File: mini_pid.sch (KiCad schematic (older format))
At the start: 68 parts, among them P1 PD Mon/Output, P2 Ext. Mod/SetPt Mon, U1 ED2610, U2 OPA2211, U3 LM2940, U4 OPA4227, U5 8DIP, U6 8DIP, U7 OPA2227

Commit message: Layout for old version completed
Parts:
- removed P2: Ext. Mod/SetPt Mon, footprints:Dual-BNC-ARF2136, symbol Dual-BNC
- added S3: spdt, footprints:CJS-1200TB-SPDT, symbol spdt
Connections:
- net GND: now also U4.5 (+); no longer U4.3 (+)
- net at C15.1, R3.1, R6.2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: now also U4.3 (+); no longer U4.5 (+)
- net at R22.2, S1.1: now also U4.7; no longer U4.1
- net at R20.2, R22.1: now also U4.6 (-); no longer U4.2 (-)
- net ext.mod.input: now reaches R4.1
- net ext.mod.input: now also S3.3
- new net: S3.1, U4.1, U4.2 (-)
- new net: P1.1, S3.2
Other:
- moved on the sheet: P1A
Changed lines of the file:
@@
 $Comp
 L OPA4227 U4
-U 2 1 58B790A6
+U 1 1 58B790A6
 P 4650 2800
 F 0 "U4" H 4700 3000 50  0000 C CNN
@@
 F 2 "Housings_SOIC:SOIC-14_3.9x8.7mm_Pitch1.27mm" H 4600 2900 50  0001 C CNN
 F 3 "" H 4700 3000 50  0000 C CNN
-	2    4650 2800
+	1    4650 2800
 	1    0    0    -1
 $EndComp
 $Comp
 L OPA4227 U4
-U 1 1 58B7910B
+U 2 1 58B7910B
 P 8350 2950
 F 0 "U4" H 8400 3150 50  0000 C CNN
@@
 F 2 "Housings_SOIC:SOIC-14_3.9x8.7mm_Pitch1.27mm" H 8300 3050 50  0001 C CNN
 F 3 "" H 8400 3150 50  0000 C CNN
-	1    8350 2950
+	2    8350 2950
 	1    0    0    -1
 $EndComp
@@
 $EndComp
 $Comp
-L Dual-BNC P2
-U 1 1 58B9ABD7
-P 3100 6050
-F 0 "P2" H 3100 6200 60  0000 C CNN
-F 1 "Ext. Mod/SetPt Mon" V 3300 5950 60  0000 C CNN
-F 2 "footprints:Dual-BNC-ARF2136" H 3100 6050 60  0001 C CNN
-F 3 "" H 3100 6050 60  0000 C CNN
-	1    3100 6050
-	-1   0    0    -1
-$EndComp
-$Comp
-L GND #PWR021
-U 1 1 58B9B8ED
-P 3100 6350
-F 0 "#PWR021" H 3100 6100 50  0001 C CNN
-F 1 "GND" H 3100 6200 50  0000 C CNN
-F 2 "" H 3100 6350 50  0000 C CNN
-F 3 "" H 3100 6350 50  0000 C CNN
-	1    3100 6350
-	1    0    0    -1
-$EndComp
-$Comp
 L R R4
 U 1 1 58B9BB14
@@
 $EndComp
 $Comp
-L GND #PWR022
+L GND #PWR021
 U 1 1 58B9F9E2
 P 3900 4900
-F 0 "#PWR022" H 3900 4650 50  0001 C CNN
+F 0 "#PWR021" H 3900 4650 50  0001 C CNN
 F 1 "GND" H 3900 4750 50  0000 C CNN
 F 2 "" H 3900 4900 50  0000 C CNN
@@
 L Dual-BNC P1
 U 1 1 58BA3D1D
-P 5400 2800
-F 0 "P1" H 5400 2950 60  0000 C CNN
-F 1 "PD Mon/Output" V 5600 2700 60  0000 C CNN
-F 2 "footprints:Dual-BNC-ARF2136" H 5400 2800 60  0001 C CNN
-F 3 "" H 5400 2800 60  0000 C CNN
-	1    5400 2800
-	1    0    0    -1
-$EndComp
-$Comp
-L GND #PWR023
+P 6650 2800
+F 0 "P1" H 6650 2950 60  0000 C CNN
+F 1 "PD Mon/Output" V 6850 2700 60  0000 C CNN
+F 2 "footprints:Dual-BNC-ARF2136" H 6650 2800 60  0001 C CNN
+F 3 "" H 6650 2800 60  0000 C CNN
+	1    6650 2800
+	1    0    0    -1
+$EndComp
+$Comp
+L GND #PWR022
 U 1 1 58BA4480
-P 5400 3100
-F 0 "#PWR023" H 5400 2850 50  0001 C CNN
-F 1 "GND" H 5400 2950 50  0000 C CNN
-F 2 "" H 5400 3100 50  0000 C CNN
-F 3 "" H 5400 3100 50  0000 C CNN
-	1    5400 3100
+P 6650 3200
+F 0 "#PWR022" H 6650 2950 50  0001 C CNN
+F 1 "GND" H 6650 3050 50  0000 C CNN
+F 2 "" H 6650 3200 50  0000 C CNN
+F 3 "" H 6650 3200 50  0000 C CNN
+	1    6650 3200
 	1    0    0    -1
 $EndComp
@@
 PI pole (Hz)\n48k\n16k\n7k\n3k\n1.6k\n700\n340\nOff
 $Comp
-L +15V #PWR024
+L +15V #PWR023
 U 1 1 58BB15C2
 P 5250 3650
-F 0 "#PWR024" H 5250 3500 50  0001 C CNN
+F 0 "#PWR023" H 5250 3500 50  0001 C CNN
 F 1 "+15V" H 5250 3790 50  0000 C CNN
 F 2 "" H 5250 3650 50  0000 C CNN
@@
 $EndComp
 $Comp
-L GND #PWR025
+L GND #PWR024
 U 1 1 58BB23F2
 P 5900 3700
-F 0 "#PWR025" H 5900 3450 50  0001 C CNN
+F 0 "#PWR024" H 5900 3450 50  0001 C CNN
 F 1 "GND" H 5900 3550 50  0000 C CNN
 F 2 "" H 5900 3700 50  0000 C CNN
@@
 $EndComp
 $Comp
-L GND #PWR026
+L GND #PWR025
 U 1 1 58BB3AC3
 P 5850 4600
-F 0 "#PWR026" H 5850 4350 50  0001 C CNN
+F 0 "#PWR025" H 5850 4350 50  0001 C CNN
 F 1 "GND" H 5850 4450 50  0000 C CNN
 F 2 "" H 5850 4600 50  0000 C CNN
@@
 $EndComp
 $Comp
-L -15V #PWR19
+L -15V #PWR18
 U 1 1 58BB5199
 P 4400 3350
-F 0 "#PWR19" H 4400 3450 50  0001 C CNN
+F 0 "#PWR18" H 4400 3450 50  0001 C CNN
 F 1 "-15V" H 4400 3500 50  0000 C CNN
 F 2 "" H 4400 3350 50  0000 C CNN
@@
 $EndComp
 $Comp
-L -15V #PWR32
+L -15V #PWR24
 U 1 1 58BB5F58
 P 5150 4600
-F 0 "#PWR32" H 5150 4700 50  0001 C CNN
+F 0 "#PWR24" H 5150 4700 50  0001 C CNN
 F 1 "-15V" H 5150 4750 50  0000 C CNN
 F 2 "" H 5150 4600 50  0000 C CNN
@@
 $EndComp
 $Comp
-L GND #PWR027
+L GND #PWR026
 U 1 1 58BB876C
 P 7650 2850
-F 0 "#PWR027" H 7650 2600 50  0001 C CNN
+F 0 "#PWR026" H 7650 2600 50  0001 C CNN
 F 1 "GND" H 7650 2700 50  0000 C CNN
 F 2 "" H 7650 2850 50  0000 C CNN
@@
 $EndComp
 $Comp
-L GND #PWR028
+L GND #PWR027
 U 1 1 58BBECAC
 P 7200 1550
-F 0 "#PWR028" H 7200 1300 50  0001 C CNN
+F 0 "#PWR027" H 7200 1300 50  0001 C CNN
 F 1 "GND" H 7200 1400 50  0000 C CNN
 F 2 "" H 7200 1550 50  0000 C CNN
@@
 $EndComp
 $Comp
-L GND #PWR029
-U 1 1 58BCC220
-P 5050 7000
-F 0 "#PWR029" H 5050 6750 50  0001 C CNN
-F 1 "GND" H 5050 6850 50  0000 C CNN
-F 2 "" H 5050 7000 50  0000 C CNN
-F 3 "" H 5050 7000 50  0000 C CNN
-	1    5050 7000
-	1    0    0    -1
-$EndComp
-$Comp
-L +15V #PWR030
+L +15V #PWR028
 U 1 1 58BCFB3C
 P 5950 750
-F 0 "#PWR030" H 5950 600 50  0001 C CNN
+F 0 "#PWR028" H 5950 600 50  0001 C CNN
 F 1 "+15V" H 5950 890 50  0000 C CNN
 F 2 "" H 5950 750 50  0000 C CNN
@@
 $EndComp
 $Comp
-L GND #PWR031
+L GND #PWR029
 U 1 1 58BD050F
 P 5950 1650
-F 0 "#PWR031" H 5950 1400 50  0001 C CNN
+F 0 "#PWR029" H 5950 1400 50  0001 C CNN
 F 1 "GND" H 5950 1500 50  0000 C CNN
 F 2 "" H 5950 1650 50  0000 C CNN
@@
 $EndComp
 $Comp
-L GND #PWR032
+L GND #PWR030
 U 1 1 58BDFB40
 P 10850 4600
-F 0 "#PWR032" H 10850 4350 50  0001 C CNN
+F 0 "#PWR030" H 10850 4350 50  0001 C CNN
 F 1 "GND" H 10850 4450 50  0000 C CNN
 F 2 "" H 10850 4600 50  0000 C CNN
@@
 $EndComp
 $Comp
-L PWR_FLAG #FLG033
+L PWR_FLAG #FLG031
 U 1 1 58BE3FE5
 P 1350 1200
-F 0 "#FLG033" H 1350 1295 50  0001 C CNN
+F 0 "#FLG031" H 1350 1295 50  0001 C CNN
 F 1 "PWR_FLAG" H 1350 1380 50  0000 C CNN
 F 2 "" H 1350 1200 50  0000 C CNN
@@
 $EndComp
 $Comp
-L PWR_FLAG #FLG034
+L PWR_FLAG #FLG032
 U 1 1 58BE4A81
 P 1000 1850
-F 0 "#FLG034" H 1000 1945 50  0001 C CNN
+F 0 "#FLG032" H 1000 1945 50  0001 C CNN
 F 1 "PWR_FLAG" H 1000 2030 50  0000 C CNN
 F 2 "" H 1000 1850 50  0000 C CNN
@@
 5V
 $Comp
-L +15V #PWR035
+L +15V #PWR033
 U 1 1 58BFDD5D
 P 3250 1200
-F 0 "#PWR035" H 3250 1050 50  0001 C CNN
+F 0 "#PWR033" H 3250 1050 50  0001 C CNN
 F 1 "+15V" H 3250 1340 50  0000 C CNN
 F 2 "" H 3250 1200 50  0000 C CNN
@@
 	1    0    0    -1
 $EndComp
-$Comp
-L Dual-BNC P2
-U 2 1 58BA3DC0
-P 5050 6600
-F 0 "P2" H 5050 6750 60  0000 C CNN
-F 1 "Ext. Mod/SetPt Mon" V 5250 6500 60  0000 C CNN
-F 2 "footprints:Dual-BNC-ARF2136" H 5050 6600 60  0001 C CNN
-F 3 "" H 5050 6600 60  0000 C CNN
-	2    5050 6600
-	1    0    0    -1
-$EndComp
 Wire Wire Line
 	1200 900  2200 900
@@
 	2600 5550 3150 5550
 Connection ~ 2850 5550
-Wire Wire Line
-	4750 4800 4750 6600
 Wire Wire Line
 	4750 4800 4450 4800
@@
 Connection ~ 6850 5200
 Wire Wire Line
-	3100 6300 3100 6350
-Wire Wire Line
 	3900 5250 4050 5250
 Wire Wire Line
 	4050 5650 4250 5650
 Wire Wire Line
-	4550 5650 4750 5650
+	4750 5650 4550 5650
 Wire Wire Line
 	3900 4900 4050 4900
@@
 	4050 4900 4050 5050
 Wire Wire Line
-	3300 6050 3550 6050
+	2900 6050 3550 6050
 Wire Wire Line
 	4050 6050 3850 6050
@@
 Connection ~ 5000 2800
 Wire Wire Line
-	5400 3050 5400 3100
+	6650 3050 6650 3200
 Wire Wire Line
 	7300 4600 7400 4600
@@
 	5250 3850 4950 3850
 Wire Wire Line
-	5050 6850 5050 7000
-Wire Wire Line
-	4750 6600 4850 6600
-Wire Wire Line
 	4950 4450 5200 4450
 Wire Wire Line
@@
 Wire Wire Line
 	5150 5050 5150 5900
+$Comp
+L spdt S3
+U 1 1 58C230CC
+P 6150 2800
+F 0 "S3" V 6300 2650 60  0000 C CNN
+F 1 "spdt" H 6150 3050 60  0000 C CNN
+F 2 "footprints:CJS-1200TB-SPDT" H 6150 2800 60  0001 C CNN
+F 3 "" H 6150 2800 60  0000 C CNN
+	1    6150 2800
+	0    -1   1    0
+$EndComp
+Wire Wire Line
+	6350 2800 6450 2800
+Wire Wire Line
+	5200 2800 5200 2600
+Wire Wire Line
+	5200 2600 6000 2600
+Text Label 5300 2950 0    60   ~ 0
+ext.mod.input
+Wire Wire Line
+	5300 2950 6000 2950
+Text Label 2900 6000 0    60   ~ 0
+ext.mod.input
+Wire Wire Line
+	2900 6000 2900 6050
+Wire Wire Line
+	4750 4800 4750 5650
 $EndSCHEMATC

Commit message: Project is now dual PID :)
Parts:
- removed C10, C12, C13, C17, C18, C19, C2, C22, C28, C29, C30, C5, C6, C7, C9: 0.1uF, Capacitors_SMD:C_0603_HandSoldering, symbol C
- removed C11, C14, C27, C3, C4: 10uF, Capacitors_SMD:C_0603_HandSoldering, symbol C
- removed C15, C8: 15pF, Capacitors_SMD:C_0603_HandSoldering, symbol C
- removed C16: 22uF, SMD_Packages:SMD-2512_Pol, symbol CP1
- removed C20: 3.3nF, Capacitors_SMD:C_0603_HandSoldering, symbol C
- removed C21: 22nF, Capacitors_SMD:C_0603_HandSoldering, symbol C
- removed C23: 0.47uF, Capacitors_SMD:C_0603_HandSoldering, symbol C
- removed C24: 10nF, Capacitors_SMD:C_0603_HandSoldering, symbol C
- removed C25: 47nF, Capacitors_SMD:C_0603_HandSoldering, symbol C
- removed C26: 0.22uF, Capacitors_SMD:C_0603_HandSoldering, symbol C
- removed D1: S5971, footprints:S5971, symbol S5971
- removed D2: TL4050B51, TO_SOT_Packages_SMD:SOT-23, symbol TL4050B51
- removed P1: PD Mon/Output, footprints:Dual-BNC-ARF2136, symbol Dual-BNC
- removed R1, R14, R3: 3.3k, Resistors_SMD:R_0603_HandSoldering, symbol R
- removed R10, R21, R4, R5, R7: 10k, Resistors_SMD:R_0603_HandSoldering, symbol R
- removed R11, R17, R18, R19, R20, R22, R23, R6, R8: 1k, Resistors_SMD:R_0603_HandSoldering, symbol R
- removed R12, R2: 100, Resistors_SMD:R_0603_HandSoldering, symbol R
- removed R13: 33k, Resistors_SMD:R_0603_HandSoldering, symbol R
- removed R15: 330, Resistors_SMD:R_0603_HandSoldering, symbol R
- removed R16, R24: 12, Resistors_SMD:R_0603_HandSoldering, symbol R
- removed R9: 100k, Resistors_SMD:R_0603_HandSoldering, symbol R
- removed RV1: 1k, footprints:VishaySpectrol536, symbol POT
- removed RV2: 10k, footprints:Bourns-PV36W104C01B00-trimmer, symbol POT
- removed S1, S2, S3: spdt, footprints:CJS-1200TB-SPDT, symbol spdt
- removed U1: ED2610, footprints:ED2610, symbol ED2610
- removed U2: OPA2211, Housings_SOIC:SOIC-8-1EP_3.9x4.9mm_Pitch1.27mm, symbol OPA2211
- removed U3: LM2940, TO_SOT_Packages_SMD:SOT-223, symbol LM2940
- removed U4: OPA4227, Housings_SOIC:SOIC-14_3.9x8.7mm_Pitch1.27mm, symbol OPA4227
- removed U5, U6: 8DIP, footprints:8_POS_DIP_Switch, symbol 8DIP
- removed U7: OPA2227, Housings_SOIC:SOIC-8_3.9x4.9mm_Pitch1.27mm, symbol OPA2227
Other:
- note removed: "PI pole (Hz)\n48k\n16k\n7k\n3k\n1.6k\n700\n340\nOff"
- note removed: "TI gain 3.3e3 V/A, Bandwidth approx 3 MHz\nlimited by feedback capacitor"
- note removed: "gains\n100\n33\n10\n2\n1\n0.33\n0.1\n0"

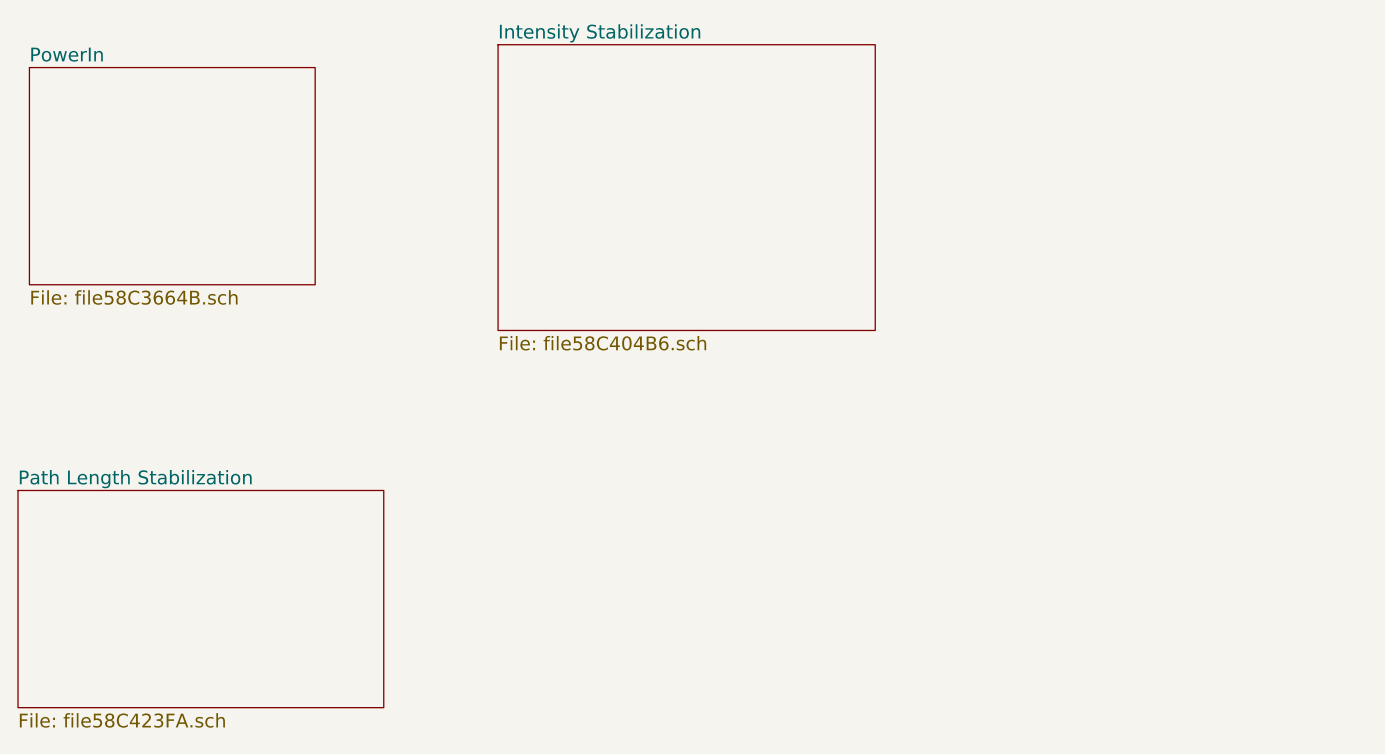
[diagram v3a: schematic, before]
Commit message: Made both circiuts identical
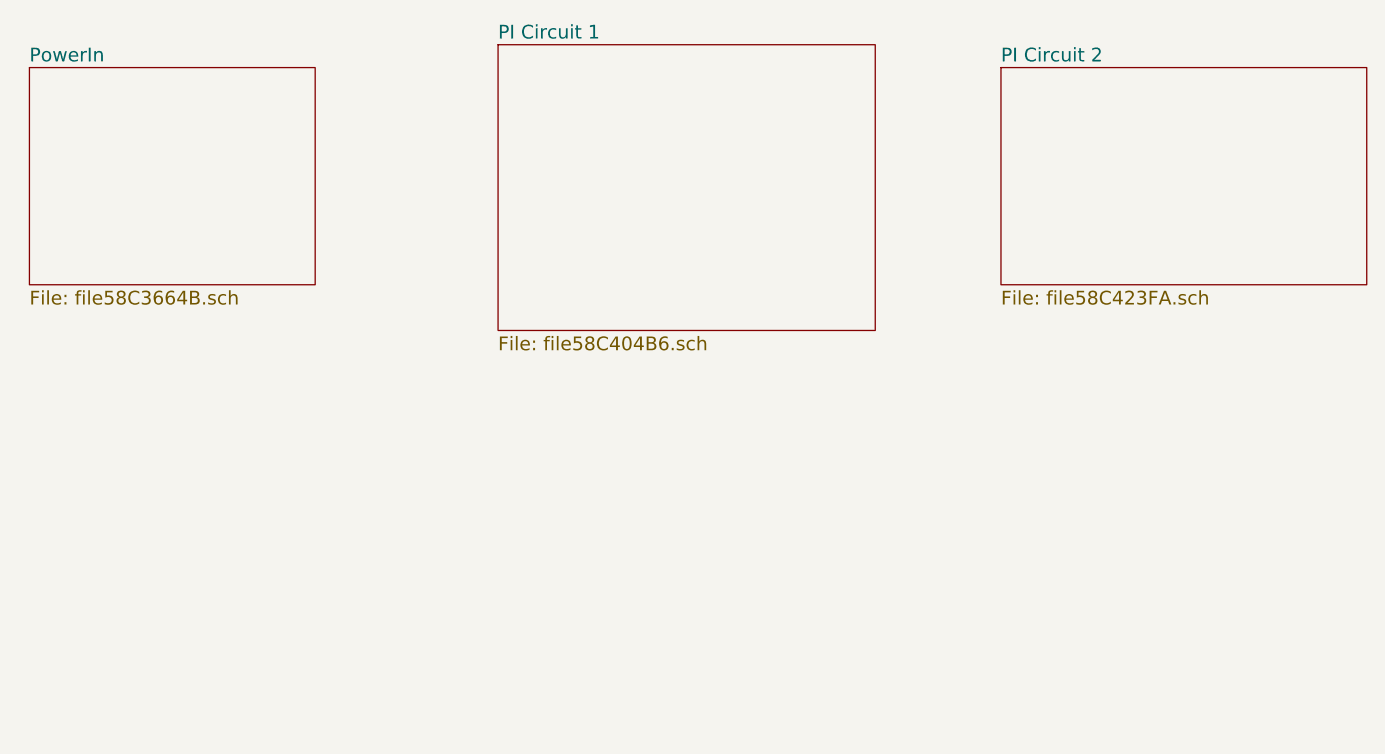
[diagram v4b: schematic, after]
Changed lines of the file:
@@
 S 3050 1050 1650 1250
 U 58C404B7
-F0 "Intensity Stabilization" 60
+F0 "PI Circuit 1" 60
 F1 "file58C404B6.sch" 60
 $EndSheet
 $Sheet
-S 950  3000 1600 950
+S 5250 1150 1600 950
 U 58C423FB
-F0 "Path Length Stabilization" 60
+F0 "PI Circuit 2" 60
 F1 "file58C423FA.sch" 60
 $EndSheet
